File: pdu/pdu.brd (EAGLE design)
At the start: 17.5 x 90 mm, 8 parts, among them IC1 FDN359BN

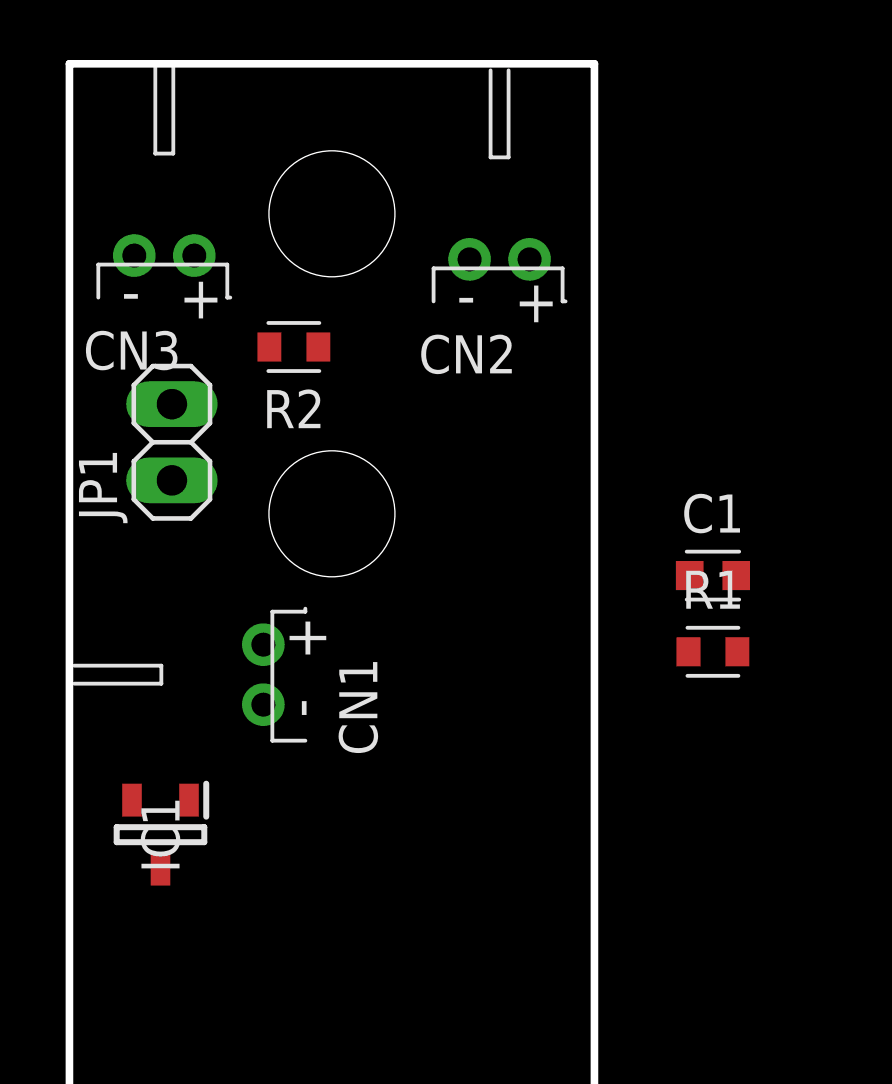
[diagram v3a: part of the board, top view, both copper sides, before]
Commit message: parallel mosfets
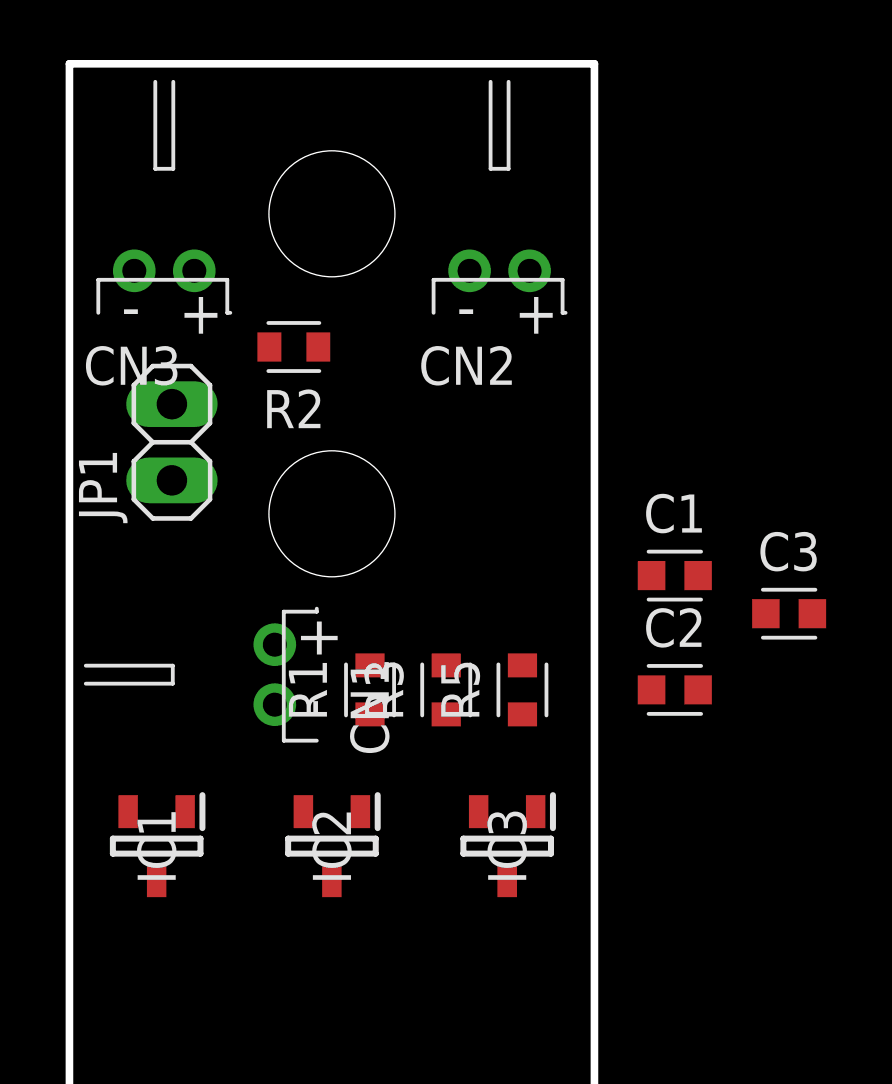
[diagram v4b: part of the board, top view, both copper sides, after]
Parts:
- added C2, C3: 100p, Capacitor:CAPC1608X85
- added IC2, IC3: FDN359BN, SamacSys_Parts:SOT95P251X112-3N
- added R3, R5: 470, Resistor:RESC1608X60
- moved R1 11.5 mm to (1.27, 24.1), turned to 90 degrees
- moved C1 1.27 mm to (11.4, 27.9)
- moved CN3 0.51 mm to (-5.59, 38.1)
- moved IC1 0.40 mm to (-5.84, 18.9)
- moved CN2 0.38 mm to (5.59, 38.1)
- moved CN1 0.38 mm to (-1.91, 24.6)
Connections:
- new net N$2: C2.2, IC2.1, R3.1
- new net N$3: C3.2, IC3.1, R5.1
- new net N$4: IC1.3, IC2.3, IC3.3
- net EN: now also R3.2, R5.2
- net GND: now also C2.1, C3.1, IC2.2, IC3.2
